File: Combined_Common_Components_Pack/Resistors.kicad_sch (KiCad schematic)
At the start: 51 parts

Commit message: More circuits
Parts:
- R3, R37, R38, R39, R40, R41, R42, R43, R44, R45, R46, R47, R48, R49, R50, R51, R52: Type SMD -> (none)
- R8: Part Number CRCW08056R8FKEA -> (none); Type SMD -> (none)
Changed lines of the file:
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@@
 			)
 		)
-		(property "Type" "SMD"
-			(at 54.61 35.56 0)
-			(effects
-				(font
-					(size 1.27 1.27)
-				)
-				(hide yes)
-			)
-		)
 		(property "Manufacturer " "UNI-ROYAL(Uniroyal Elec)"
 			(at 54.61 35.56 0)
@@
 			)
 		)
-		(property "Type" "SMD"
-			(at 72.39 35.56 0)
-			(effects
-				(font
-					(size 1.27 1.27)
-				)
-				(hide yes)
-			)
-		)
 		(property "Manufacturer " "UNI-ROYAL(Uniroyal Elec)"
 			(at 72.39 35.56 0)
@@
 			)
 		)
-		(property "Type" "SMD"
-			(at 63.5 35.56 0)
-			(effects
-				(font
-					(size 1.27 1.27)
-				)
-				(hide yes)
-			)
-		)
 		(property "Manufacturer " "UNI-ROYAL(Uniroyal Elec)"
 			(at 63.5 35.56 0)
@@
 			)
 		)
-		(property "Type" "SMD"
-			(at 72.39 58.42 0)
-			(effects
-				(font
-					(size 1.27 1.27)
-				)
-				(hide yes)
-			)
-		)
 		(property "Manufacturer " "UNI-ROYAL(Uniroyal Elec)"
 			(at 72.39 58.42 0)
@@
 			)
 		)
-		(property "Type" "SMD"
-			(at 45.72 46.99 0)
-			(effects
-				(font
-					(size 1.27 1.27)
-				)
-				(hide yes)
-			)
-		)
 		(property "Manufacturer " "UNI-ROYAL(Uniroyal Elec)"
 			(at 45.72 46.99 0)
@@
 			)
 		)
-		(property "Type" "SMD"
-			(at 27.94 46.99 0)
-			(effects
-				(font
-					(size 1.27 1.27)
-				)
-				(hide yes)
-			)
-		)
 		(property "Manufacturer " "UNI-ROYAL(Uniroyal Elec)"
 			(at 27.94 46.99 0)
@@
 			)
 		)
-		(property "Type" "SMD"
-			(at 45.72 58.42 0)
-			(effects
-				(font
-					(size 1.27 1.27)
-				)
-				(hide yes)
-			)
-		)
 		(property "Manufacturer " "UNI-ROYAL(Uniroyal Elec)"
 			(at 45.72 58.42 0)
@@
 			)
 		)
-		(property "Type" "SMD"
-			(at 27.94 71.12 0)
-			(effects
-				(font
-					(size 1.27 1.27)
-				)
-				(hide yes)
-			)
-		)
 		(property "Manufacturer " "UNI-ROYAL(Uniroyal Elec)"
 			(at 27.94 71.12 0)
@@
 			)
 		)
-		(property "Type" "SMD"
-			(at 27.94 58.42 0)
-			(effects
-				(font
-					(size 1.27 1.27)
-				)
-				(hide yes)
-			)
-		)
 		(property "Manufacturer " "UNI-ROYAL(Uniroyal Elec)"
 			(at 27.94 58.42 0)
@@
 			)
 		)
-		(property "Type" "SMD"
-			(at 63.5 58.42 0)
-			(effects
-				(font
-					(size 1.27 1.27)
-				)
-				(hide yes)
-			)
-		)
 		(property "Manufacturer " "UNI-ROYAL(Uniroyal Elec)"
 			(at 63.5 58.42 0)
@@
 			)
 		)
-		(property "Part Number" "CRCW08056R8FKEA"
-			(at 241.3 43.18 0)
-			(effects
-				(font
-					(size 1.27 1.27)
-				)
-				(hide yes)
-			)
-		)
-		(property "Type" "SMD"
-			(at 241.3 43.18 0)
-			(effects
-				(font
-					(size 1.27 1.27)
-				)
-				(hide yes)
-			)
-		)
 		(property "Manufacturer " "FOJAN"
 			(at 241.3 43.18 0)
@@
 			)
 		)
-		(property "Supplier" ""
-			(at 241.3 43.18 0)
-			(effects
-				(font
-					(size 1.27 1.27)
-				)
-				(hide yes)
-			)
-		)
-		(property "Package" ""
-			(at 241.3 43.18 0)
-			(effects
-				(font
-					(size 1.27 1.27)
-				)
-				(hide yes)
-			)
-		)
 		(property "LCSC" "C3013311"
 			(at 241.3 43.18 0)
@@
 			)
 		)
-		(property "Type" "SMD"
-			(at 54.61 58.42 0)
-			(effects
-				(font
-					(size 1.27 1.27)
-				)
-				(hide yes)
-			)
-		)
 		(property "Manufacturer " "UNI-ROYAL(Uniroyal Elec)"
 			(at 54.61 58.42 0)
@@
 			)
 		)
-		(property "Type" "SMD"
-			(at 36.83 58.42 0)
-			(effects
-				(font
-					(size 1.27 1.27)
-				)
-				(hide yes)
-			)
-		)
 		(property "Manufacturer " "UNI-ROYAL(Uniroyal Elec)"
 			(at 36.83 58.42 0)
@@
 			)
 		)
-		(property "Type" "SMD"
-			(at 55.88 71.12 0)
-			(effects
-				(font
-					(size 1.27 1.27)
-				)
-				(hide yes)
-			)
-		)
 		(property "Manufacturer " "UNI-ROYAL(Uniroyal Elec)"
 			(at 55.88 71.12 0)
@@
 			)
 		)
-		(property "Type" "SMD"
-			(at 36.83 46.99 0)
-			(effects
-				(font
-					(size 1.27 1.27)
-				)
-				(hide yes)
-			)
-		)
 		(property "Manufacturer " "UNI-ROYAL(Uniroyal Elec)"
 			(at 36.83 46.99 0)
@@
 			)
 		)
-		(property "Type" "SMD"
-			(at 81.28 58.42 0)
-			(effects
-				(font
-					(size 1.27 1.27)
-				)
-				(hide yes)
-			)
-		)
 		(property "Manufacturer " "UNI-ROYAL(Uniroyal Elec)"
 			(at 81.28 58.42 0)
@@
 			)
 		)
-		(property "Type" "SMD"
-			(at 27.94 35.56 0)
-			(effects
-				(font
-					(size 1.27 1.27)
-				)
-				(hide yes)
-			)
-		)
 		(property "Manufacturer " "UNI-ROYAL(Uniroyal Elec)"
 			(at 27.94 35.56 0)
@@
 			(at 45.72 35.56 0)
 			(effects
-				(font
-					(size 1.27 1.27)
-				)
-				(hide yes)
-			)
-		)
-		(property "Type" "SMD"
-			(at 45.72 35.56 0)
-			(effects

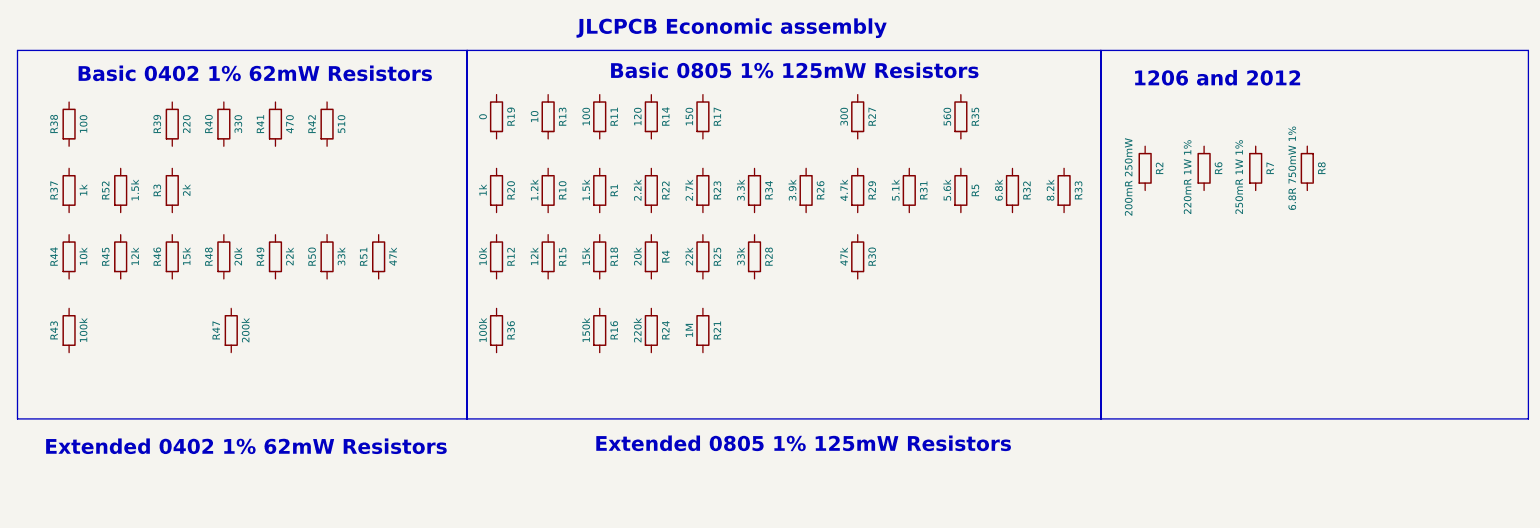
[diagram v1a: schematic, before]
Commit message: Minor updates
Basically components annotation, and more basic parts added
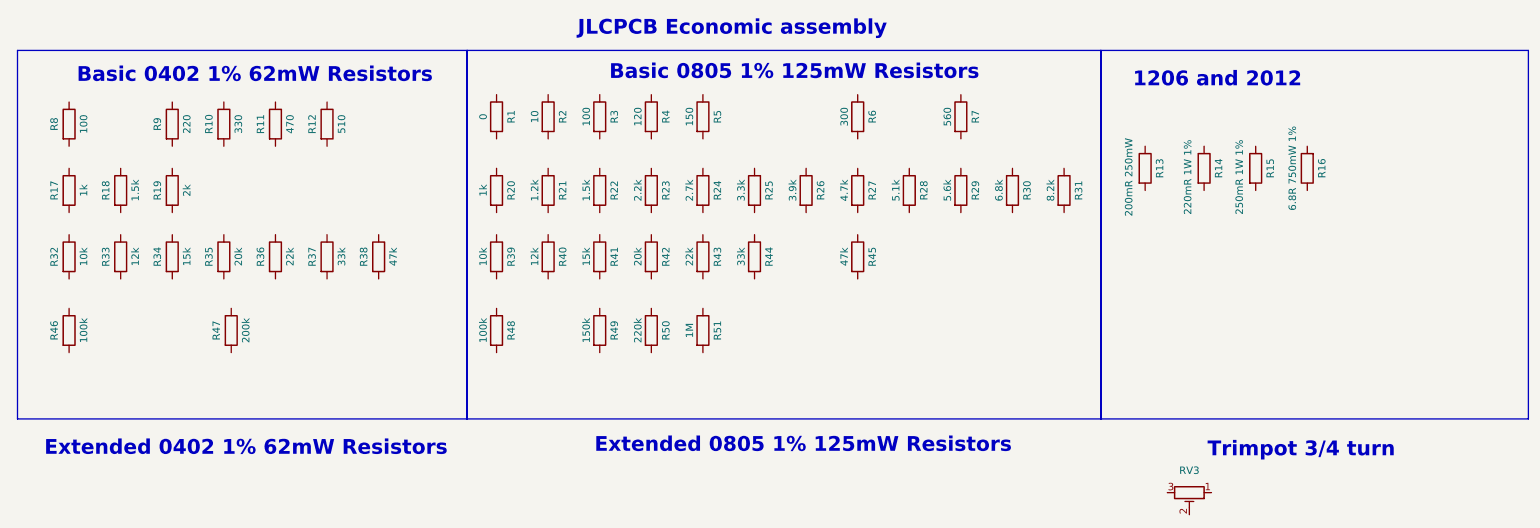
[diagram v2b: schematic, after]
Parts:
- added RV3: 10k, Potentiometer_THT:Potentiometer_Runtron_RM-065_Vertical, symbol Device:R_Potentiometer_Trim
- renumbered R19 to R1, R40 to R10, R41 to R11, R42 to R12, R2 to R13, R6 to R14, R7 to R15, R8 to R16, R37 to R17, R52 to R18, R3 to R19, R13 to R2, R10 to R21, R1 to R22, R22 to R23, R23 to R24, R34 to R25, R29 to R27, R31 to R28, R5 to R29, R11 to R3, R32 to R30, R33 to R31, R44 to R32, R45 to R33, R46 to R34, R48 to R35, R49 to R36, R50 to R37, R51 to R38, R12 to R39, R14 to R4, R15 to R40, R18 to R41, R4 to R42, R25 to R43, R28 to R44, R30 to R45, R43 to R46, R36 to R48, R16 to R49, R17 to R5, R24 to R50, R21 to R51, R27 to R6, R35 to R7, R38 to R8, R39 to R9
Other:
- note added: "Trimpot 3/4 turn"
